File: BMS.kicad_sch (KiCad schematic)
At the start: 0 parts

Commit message: almost completed scheamtic
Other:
- added sheet main (main.kicad_sch)
- added sheet main1 (main.kicad_sch)
- added sheet pcb (pcb.kicad_sch)
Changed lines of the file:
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@@
 	(generator_version "9.0")
 	(paper "A4")
+	(sheet
+		(at 48.26 44.45)
+		(size 39.37 15.24)
+		(exclude_from_sim no)
+		(in_bom yes)
+		(on_board yes)
+		(dnp no)
+		(fields_autoplaced yes)
+		(stroke
+			(width 0.1524)
+			(type solid)
+			(color 0 0 0 1)
+		)
+		(fill
+			(color 31 138 58 1.0000)
+		)
+		(property "Sheetname" "main"
+			(at 48.26 43.7384 0)
+			(effects
+				(font
+					(size 1.27 1.27)
+				)
+				(justify left bottom)
+			)
+		)
+		(property "Sheetfile" "main.kicad_sch"
+			(at 48.26 60.2746 0)
+			(effects
+				(font
+					(size 1.27 1.27)
+				)
+				(justify left top)
+			)
+		)
+		(instances
+			(project "BMS"
+				(path "/124184ba-5d68-4d9f-8da6-acc6720ab30b"
+					(page "2")
+				)
+			)
+		)
+	)
+	(sheet
+		(at 49.53 74.93)
+		(size 39.37 15.24)
+		(exclude_from_sim no)
+		(in_bom yes)
+		(on_board yes)
+		(dnp no)
+		(fields_autoplaced yes)
+		(stroke
+			(width 0.1524)
+			(type solid)
+			(color 0 0 0 1)
+		)
+		(fill
+			(color 31 138 58 1.0000)
+		)
+		(property "Sheetname" "main1"
+			(at 49.53 74.2184 0)
+			(effects
+				(font
+					(size 1.27 1.27)
+				)
+				(justify left bottom)
+			)
+		)
+		(property "Sheetfile" "main.kicad_sch"
+			(at 49.53 90.7546 0)
+			(effects
+				(font
+					(size 1.27 1.27)
+				)
+				(justify left top)
+			)
+		)
+		(instances
+			(project "BMS"
+				(path "/124184ba-5d68-4d9f-8da6-acc6720ab30b"
+					(page "4")
+				)
+			)
+		)
+	)
+	(sheet
+		(at 111.76 44.45)
+		(size 40.64 15.24)
+		(exclude_from_sim no)
+		(in_bom yes)
+		(on_board yes)
+		(dnp no)
+		(fields_autoplaced yes)
+		(stroke
+			(width 0.1524)
+			(type solid)
+			(color 0 0 0 1)
+		)
+		(fill
+			(color 31 138 58 1.0000)
+		)
+		(property "Sheetname" "pcb"
+			(at 111.76 43.7384 0)
+			(effects
+				(font
+					(size 1.27 1.27)
+				)
+				(justify left bottom)
+			)
+		)
+		(property "Sheetfile" "pcb.kicad_sch"
+			(at 111.76 60.2746 0)
+			(effects
+				(font
+					(size 1.27 1.27)
+				)
+				(justify left top)
+			)
+		)
+		(instances
+			(project "BMS"
+				(path "/124184ba-5d68-4d9f-8da6-acc6720ab30b"
+					(page "3")
+				)
+			)
+		)
+	)
 	(sheet_instances
 		(path "/"

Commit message: post solar meeting with ezzat
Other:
- removed sheet main1
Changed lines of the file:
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@@
 	(paper "A4")
-	(sheet
-		(at 48.26 44.45)
-		(size 39.37 15.24)
-		(exclude_from_sim no)
-		(in_bom yes)
-		(on_board yes)
-		(dnp no)
-		(fields_autoplaced yes)
-		(stroke
-			(width 0.1524)
-			(type solid)
-			(color 0 0 0 1)
-		)
-		(fill
-			(color 31 138 58 1.0000)
-		)
-		(property "Sheetname" "main"
-			(at 48.26 43.7384 0)
-			(effects
-				(font
-					(size 1.27 1.27)
-				)
-				(justify left bottom)
-			)
-		)
-		(property "Sheetfile" "main.kicad_sch"
-			(at 48.26 60.2746 0)
-			(effects
-				(font
-					(size 1.27 1.27)
-				)
-				(justify left top)
-			)
-		)
-		(instances
-			(project "BMS"
-				(path "/124184ba-5d68-4d9f-8da6-acc6720ab30b"
-					(page "2")
-				)
-			)
-		)
-	)
 	(sheet
 		(at 49.53 74.93)
@@
 			(color 31 138 58 1.0000)
 		)
-		(property "Sheetname" "main1"
+		(property "Sheetname" "main"
 			(at 49.53 74.2184 0)
 			(effects

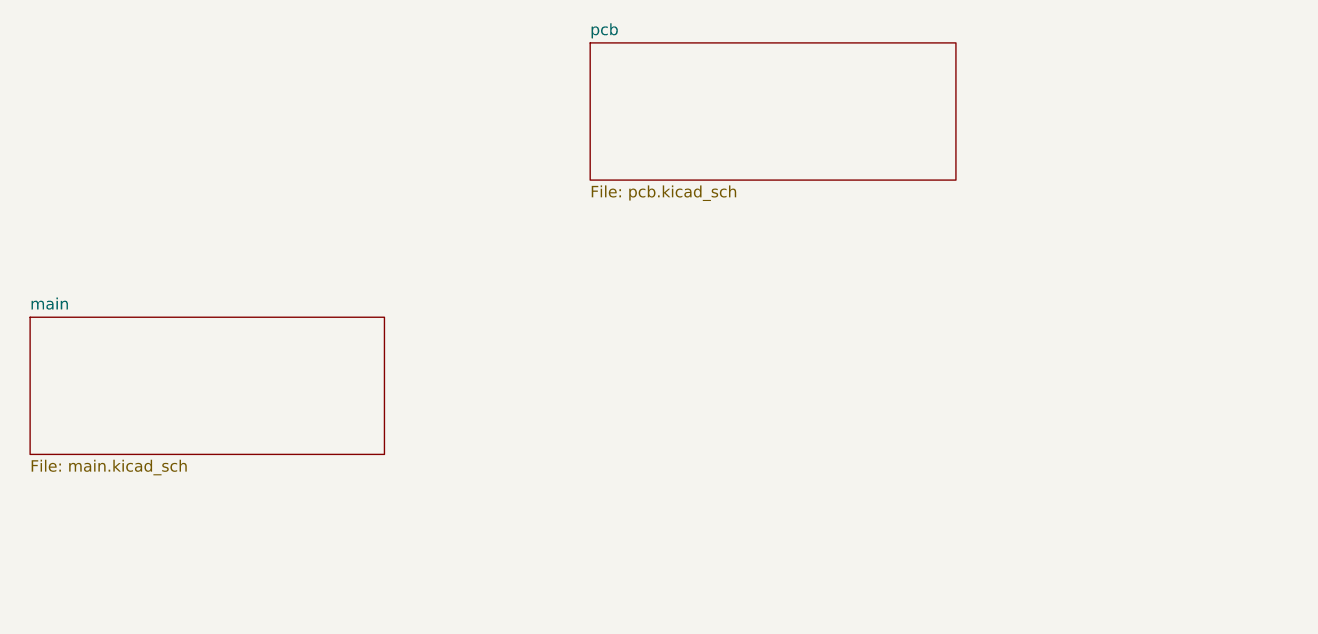
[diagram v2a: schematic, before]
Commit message: Fixing and cleaning up schematic
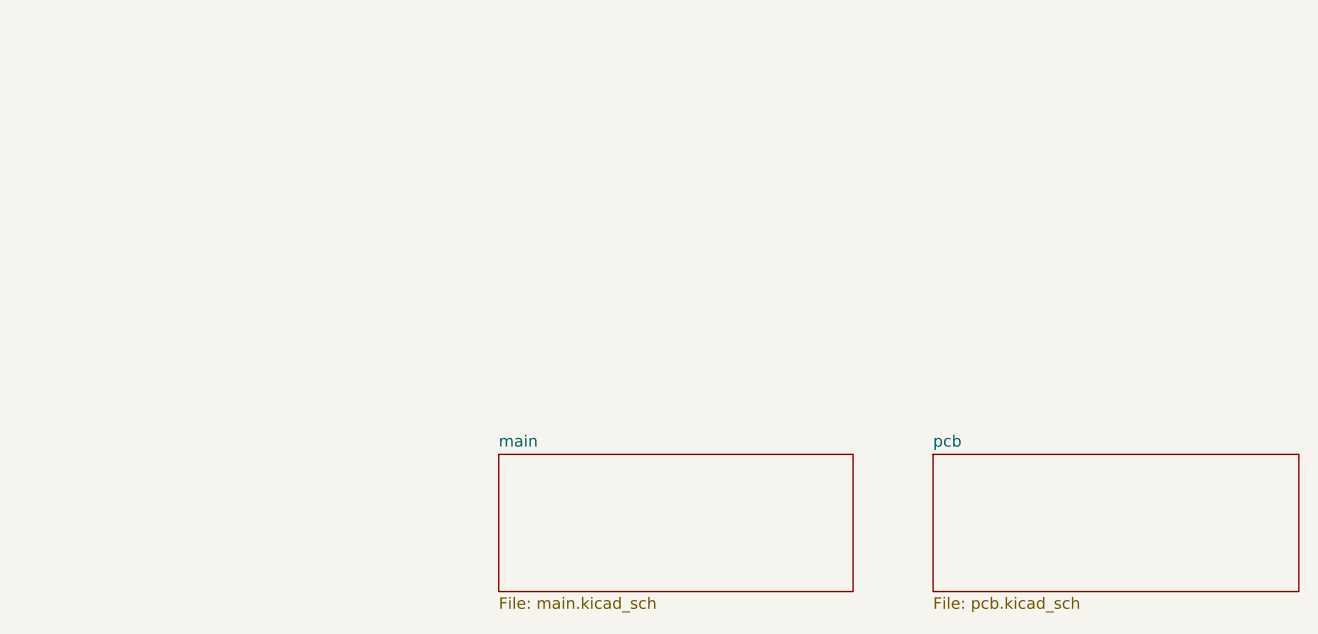
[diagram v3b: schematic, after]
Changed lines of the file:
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@@
 	(generator_version "9.0")
 	(paper "A4")
+	(bus_alias "I2C"
+		(members "SDA" "SCL")
+	)
 	(sheet
-		(at 49.53 74.93)
+		(at 101.6 90.17)
 		(size 39.37 15.24)
 		(exclude_from_sim no)
@@
 		)
 		(fill
-			(color 31 138 58 1.0000)
+			(color 0 194 0 1.0000)
 		)
 		(property "Sheetname" "main"
-			(at 49.53 74.2184 0)
+			(at 101.6 89.4584 0)
 			(effects
 				(font
@@
 		)
 		(property "Sheetfile" "main.kicad_sch"
-			(at 49.53 90.7546 0)
+			(at 101.6 105.9946 0)
 			(effects
 				(font
@@
 	)
 	(sheet
-		(at 111.76 44.45)
+		(at 149.86 90.17)
 		(size 40.64 15.24)
 		(exclude_from_sim no)
@@
 		)
 		(fill
-			(color 31 138 58 1.0000)
+			(color 0 194 0 1.0000)
 		)
 		(property "Sheetname" "pcb"
-			(at 111.76 43.7384 0)
+			(at 149.86 89.4584 0)
 			(effects
 				(font
@@
 		)
 		(property "Sheetfile" "pcb.kicad_sch"
-			(at 111.76 60.2746 0)
+			(at 149.86 105.9946 0)
 			(effects
 				(font
